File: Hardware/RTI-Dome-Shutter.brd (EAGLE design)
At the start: 80 x 71.1 mm, 42 parts, among them IC1 24AA128ST, IC5 74LVC245, IC6 74ABT245, J1 POWERPOLE_POWER45A

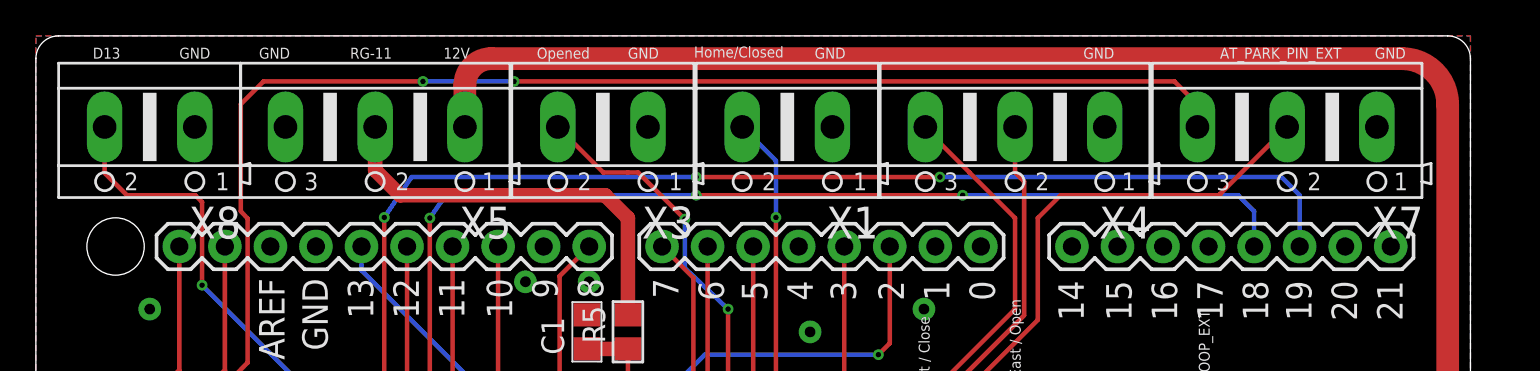
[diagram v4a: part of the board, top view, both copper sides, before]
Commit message: Better homing code. Does necessarily stop at home bug sinf home via an interrupt. I'll add more got to go back home after passing it. It does however return the proper position after homing. Added more board for ENC424J600 ethernet chip. Fix position of the headers.
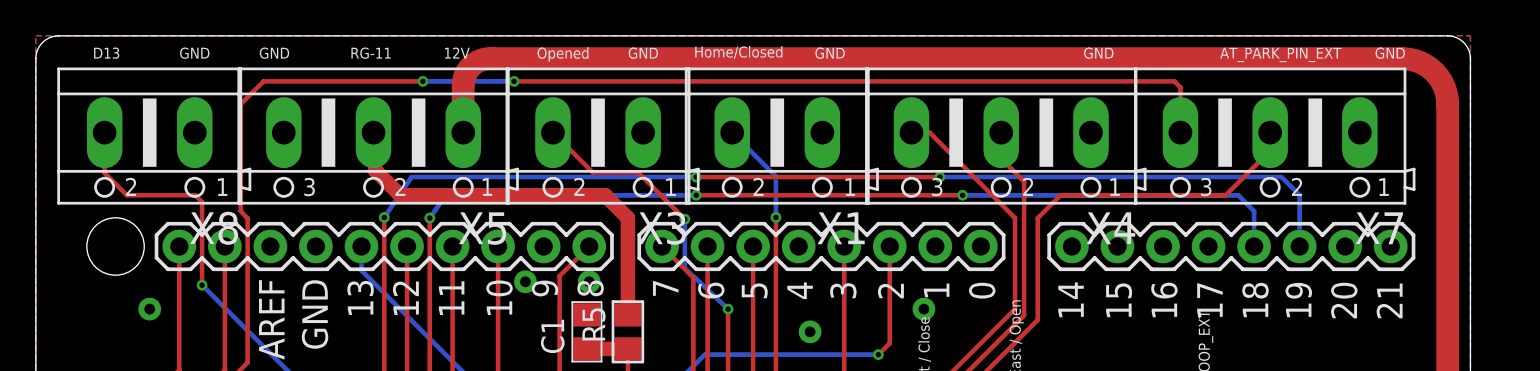
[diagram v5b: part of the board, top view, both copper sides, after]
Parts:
- moved X7 1.00 mm to (68.8, 65.7)
- moved X4 0.83 mm to (53.8, 65.7)
- moved X1 0.64 mm to (41.4, 65.7)
- moved X3 0.42 mm to (31.4, 65.7)
- moved X5 0.33 mm to (18.8, 65.7)
- moved X8 0.32 mm to (6.35, 65.7)
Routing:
- net BUTTON_WEST_CLOSE_5V: track 48.7 -> 49.3 mm
- net AT_PARK_PIN_EXT: track 59.3 -> 58.8 mm

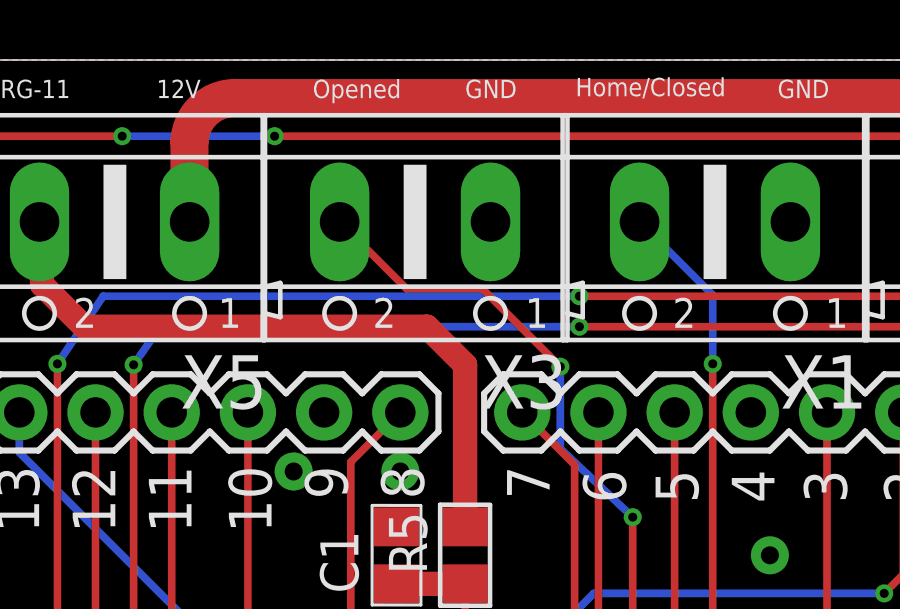
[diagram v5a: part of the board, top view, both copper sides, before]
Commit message: Fix all board for proper header alignement. New code for homing (and calibrating) tested and works.
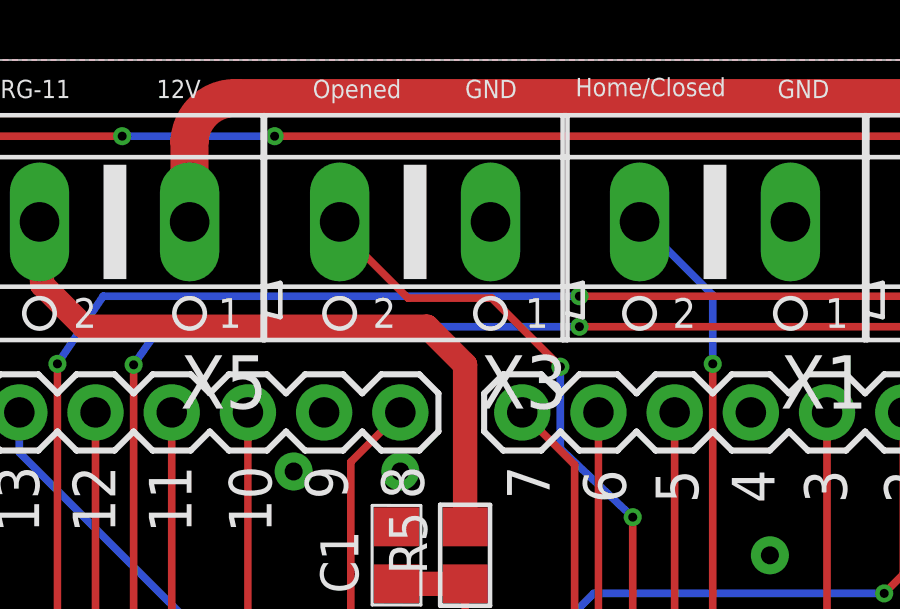
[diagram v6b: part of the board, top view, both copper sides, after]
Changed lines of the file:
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@@
 <setting verticaltext="up"/>
 </settings>
-<grid distance="0.3175" unitdist="mm" unit="mm" style="lines" multiple="1" display="yes" altdistance="0.03175" altunitdist="mm" altunit="mm"/>
+<grid distance="0.3175" unitdist="mm" unit="mm" style="lines" multiple="1" display="no" altdistance="0.03175" altunitdist="mm" altunit="mm"/>
 <layers>
 <layer number="1" name="Top" color="4" fill="1" visible="yes" active="yes"/>
@@
 <wire x1="41.37025" y1="31.71825" x2="42.19575" y2="30.89275" width="0.254" layer="1"/>
 <wire x1="42.19575" y1="30.89275" x2="42.19575" y2="29.779" width="0.254" layer="1"/>
-<wire x1="33.5915" y1="63.5" x2="36.195" y2="60.8965" width="0.254" layer="1"/>
 <via x="36.195" y="60.8965" extent="1-16" drill="0.3" diameter="0.254"/>
 <wire x1="36.195" y1="60.8965" x2="36.195" y2="58.166" width="0.254" layer="16"/>
@@
 <wire x1="39.37" y1="43.18" x2="39.37" y2="36.22675" width="0.254" layer="16"/>
 <wire x1="39.37" y1="36.22675" x2="38.481" y2="35.33775" width="0.254" layer="16"/>
-<wire x1="28.8384" y1="65.7225" x2="31.0609" y2="63.5" width="0.254" layer="1"/>
-<wire x1="31.0609" y1="63.5" x2="33.5915" y2="63.5" width="0.254" layer="1"/>
+<wire x1="36.195" y1="60.8965" x2="33.909" y2="63.1825" width="0.254" layer="1"/>
+<wire x1="33.909" y1="63.1825" x2="31.115" y2="63.1825" width="0.254" layer="1"/>
+<wire x1="31.115" y1="63.1825" x2="28.8384" y2="65.4591" width="0.254" layer="1"/>
+<wire x1="28.8384" y1="65.4591" x2="28.8384" y2="65.7225" width="0.254" layer="1"/>
 </signal>
 <signal name="HOME_SHUTTER_CLOSED_5V">

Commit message: Fix some componenent manufacturer reference
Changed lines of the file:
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@@
 </class>
 </classes>
-<designrules name="Fusion">
-<description language="de">&lt;b&gt;EAGLE Design Rules&lt;/b&gt;
+<designrules name="jlcpcb2layer">
+<description language="en">&lt;b&gt;JLCPCB Design Rules by Jaap de Dood&lt;/b&gt;
 &lt;p&gt;
-Die Standard-Design-Rules sind so gewÃÂÃÂ¤hlt, dass sie fÃÂÃÂ¼r
-die meisten Anwendungen passen. Sollte ihre Platine
-besondere Anforderungen haben, treffen Sie die erforderlichen
-Einstellungen hier und speichern die Design Rules unter
-einem neuen Namen ab.</description>
-<description language="en">&lt;b&gt;EAGLE Design Rules&lt;/b&gt;
-&lt;p&gt;
-The default Design Rules have been set to cover
-a wide range of applications. Your particular design
-may have different requirements, so please make the
-necessary adjustments and save your customized
-design rules under a new name.</description>
+Please make sure your boards conform to these design rules.
+&lt;/p&gt;</description>
 <param name="layerSetup" value="(1*16)"/>
-<param name="mtCopper" value="0.07mm 0.035mm 0.035mm 0.035mm 0.035mm 0.035mm 0.035mm 0.035mm 0.035mm 0.035mm 0.035mm 0.035mm 0.035mm 0.035mm 0.035mm 0.07mm"/>
-<param name="mtIsolate" value="1.6mm 0.5mm 0.25mm 0.15mm 0.2mm 0.15mm 0.2mm 0.15mm 0.2mm 0.15mm 0.2mm 0.15mm 0.2mm 0.25mm 0.5mm"/>
-<param name="mdWireWire" value="8mil"/>
-<param name="mdWirePad" value="8mil"/>
-<param name="mdWireVia" value="8mil"/>
-<param name="mdPadPad" value="8mil"/>
-<param name="mdPadVia" value="8mil"/>
-<param name="mdViaVia" value="8mil"/>
-<param name="mdSmdPad" value="6mil"/>
-<param name="mdSmdVia" value="6mil"/>
-<param name="mdSmdSmd" value="6mil"/>
+<param name="mtCopper" value="0.035mm 0.035mm 0.035mm 0.035mm 0.035mm 0.035mm 0.035mm 0.035mm 0.035mm 0.035mm 0.035mm 0.035mm 0.035mm 0.035mm 0.035mm 0.035mm"/>
+<param name="mtIsolate" value="1.6mm 0.15mm 0.2mm 0.15mm 0.2mm 0.15mm 0.2mm 0.15mm 0.2mm 0.15mm 0.2mm 0.15mm 0.2mm 0.15mm 0.2mm"/>
+<param name="mdWireWire" value="5mil"/>
+<param name="mdWirePad" value="5mil"/>
+<param name="mdWireVia" value="5mil"/>
+<param name="mdPadPad" value="5mil"/>
+<param name="mdPadVia" value="5mil"/>
+<param name="mdViaVia" value="5mil"/>
+<param name="mdSmdPad" value="5mil"/>
+<param name="mdSmdVia" value="5mil"/>
+<param name="mdSmdSmd" value="5mil"/>
 <param name="mdViaViaSameLayer" value="8mil"/>
 <param name="mnLayersViaInSmd" value="2"/>
-<param name="mdCopperDimension" value="13mil"/>
-<param name="mdDrill" value="6mil"/>
+<param name="mdCopperDimension" value="8mil"/>
+<param name="mdDrill" value="0.5mm"/>
 <param name="mdSmdStop" value="0mil"/>
-<param name="msWidth" value="8mil"/>
-<param name="msDrill" value="0.3mm"/>
-<param name="msMicroVia" value="8mil"/>
+<param name="msWidth" value="5mil"/>
+<param name="msDrill" value="0.2mm"/>
+<param name="msMicroVia" value="0.2mm"/>
 <param name="msBlindViaRatio" value="0.5"/>
 <param name="rvPadTop" value="0.25"/>
@@
 <param name="rvMicroViaOuter" value="0.25"/>
 <param name="rvMicroViaInner" value="0.25"/>
-<param name="rlMinPadTop" value="6mil"/>
+<param name="rlMinPadTop" value="0.13mm"/>
 <param name="rlMaxPadTop" value="20mil"/>
-<param name="rlMinPadInner" value="6mil"/>
+<param name="rlMinPadInner" value="0.13mm"/>
 <param name="rlMaxPadInner" value="20mil"/>
-<param name="rlMinPadBottom" value="6mil"/>
+<param name="rlMinPadBottom" value="0.13mm"/>
 <param name="rlMaxPadBottom" value="20mil"/>
-<param name="rlMinViaOuter" value="6mil"/>
+<param name="rlMinViaOuter" value="0.13mm"/>
 <param name="rlMaxViaOuter" value="20mil"/>
-<param name="rlMinViaInner" value="6mil"/>
+<param name="rlMinViaInner" value="0.13mm"/>
 <param name="rlMaxViaInner" value="20mil"/>
-<param name="rlMinMicroViaOuter" value="6mil"/>
+<param name="rlMinMicroViaOuter" value="0.13mm"/>
 <param name="rlMaxMicroViaOuter" value="20mil"/>
-<param name="rlMinMicroViaInner" value="6mil"/>
+<param name="rlMinMicroViaInner" value="0.13mm"/>
 <param name="rlMaxMicroViaInner" value="20mil"/>
 <param name="psTop" value="-1"/>
@@
 <param name="mvStopFrame" value="1"/>
 <param name="mvCreamFrame" value="0"/>
-<param name="mlMinStopFrame" value="3mil"/>
-<param name="mlMaxStopFrame" value="3mil"/>
-<param name="mlMinCreamFrame" value="0mil"/>
+<param name="mlMinStopFrame" value="0.05mm"/>
+<param name="mlMaxStopFrame" value="2.5mil"/>
+<param name="mlMinCreamFrame" value="0.05mm"/>
 <param name="mlMaxCreamFrame" value="0mil"/>
-<param name="mlViaStopLimit" value="130mil"/>
+<param name="mlViaStopLimit" value="40mil"/>
 <param name="srRoundness" value="0"/>
 <param name="srMinRoundness" value="0mil"/>
 <param name="srMaxRoundness" value="0mil"/>
-<param name="slThermalIsolate" value="8mil"/>
+<param name="slThermalIsolate" value="10mil"/>
 <param name="slThermalsForVias" value="0"/>
 <param name="dpMaxLengthDifference" value="10mm"/>
@@
 <param name="checkFont" value="1"/>
 <param name="checkRestrict" value="1"/>
-<param name="useDiameter" value="31"/>
+<param name="useDiameter" value="13"/>
 <param name="maxErrors" value="50"/>
 </designrules>
